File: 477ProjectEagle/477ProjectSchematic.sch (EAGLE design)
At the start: 67 parts, among them J1 POWER_JACK_BAT, J2 POWER_JACK_12VOUT, Q1 AO4419, X1 22-23-2051, X10 MOTORS, X2 XRJK-S-01-6-6-0-2G2-NO

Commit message: Scott lab -- Work on main PCB
Started connecting everything together. Made a bunch of progress.
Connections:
- net +3V3: now also X1-1.S; no longer X1-2.S
- net GND: now also X1-2.S; no longer X1-1.S
- net N$12: now also U$3.A1
- net N$13: now also U$3.A2
- net N$8: now also U$19.A8; no longer U$19.A7
- net N$9: now also U$19.A7; no longer U$19.A8
- net SCL: now also U$3.B1
- net SDA: now also U$3.B2
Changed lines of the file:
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@@
 <instance part="SUPPLY38" gate="+5V" x="-83.82" y="7.62"/>
 <instance part="SUPPLY39" gate="GND" x="-86.36" y="-5.08"/>
-<instance part="SUPPLY40" gate="GND" x="-426.72" y="10.16"/>
+<instance part="SUPPLY40" gate="GND" x="-429.26" y="10.16"/>
 <instance part="+3V2" gate="G$1" x="-132.08" y="73.66"/>
 <instance part="+3V3" gate="G$1" x="-167.64" y="-12.7"/>
@@
 <segment>
 <pinref part="U$1" gate="A" pin="U1RX/SDI1/RF2"/>
-<wire x1="76.2" y1="-27.94" x2="83.82" y2="-27.94" width="0.1524" layer="91"/>
-<wire x1="83.82" y1="-27.94" x2="99.06" y2="-27.94" width="0.1524" layer="91"/>
-<wire x1="99.06" y1="-27.94" x2="99.06" y2="33.02" width="0.1524" layer="91"/>
-<pinref part="U$19" gate="G$1" pin="A7"/>
-<wire x1="99.06" y1="33.02" x2="106.68" y2="33.02" width="0.1524" layer="91"/>
+<wire x1="76.2" y1="-27.94" x2="99.06" y2="-27.94" width="0.1524" layer="91"/>
+<wire x1="99.06" y1="-27.94" x2="99.06" y2="30.48" width="0.1524" layer="91"/>
 <junction x="76.2" y="-27.94"/>
-<junction x="106.68" y="33.02"/>
+<pinref part="U$19" gate="G$1" pin="A8"/>
+<wire x1="99.06" y1="30.48" x2="106.68" y2="30.48" width="0.1524" layer="91"/>
+<junction x="106.68" y="30.48"/>
 </segment>
 </net>
 <net name="N$9" class="0">
 <segment>
-<wire x1="81.28" y1="-30.48" x2="76.2" y2="-30.48" width="0.1524" layer="91"/>
-<pinref part="U$19" gate="G$1" pin="A8"/>
 <wire x1="76.2" y1="-30.48" x2="73.66" y2="-30.48" width="0.1524" layer="91"/>
-<wire x1="106.68" y1="30.48" x2="101.6" y2="30.48" width="0.1524" layer="91"/>
-<wire x1="101.6" y1="30.48" x2="101.6" y2="-30.48" width="0.1524" layer="91"/>
-<wire x1="101.6" y1="-30.48" x2="81.28" y2="-30.48" width="0.1524" layer="91"/>
+<wire x1="101.6" y1="33.02" x2="101.6" y2="-30.48" width="0.1524" layer="91"/>
+<wire x1="101.6" y1="-30.48" x2="76.2" y2="-30.48" width="0.1524" layer="91"/>
 <pinref part="U$1" gate="A" pin="U1TX/SDO1/RF3"/>
 <junction x="76.2" y="-30.48"/>
-<junction x="106.68" y="30.48"/>
+<pinref part="U$19" gate="G$1" pin="A7"/>
+<wire x1="101.6" y1="33.02" x2="106.68" y2="33.02" width="0.1524" layer="91"/>
+<junction x="106.68" y="33.02"/>
 </segment>
 </net>
@@
 <wire x1="76.2" y1="-20.32" x2="132.08" y2="-20.32" width="0.1524" layer="91"/>
 <wire x1="132.08" y1="-20.32" x2="132.08" y2="-58.42" width="0.1524" layer="91"/>
-<wire x1="132.08" y1="-58.42" x2="144.78" y2="-58.42" width="0.1524" layer="91"/>
+<wire x1="132.08" y1="-58.42" x2="142.24" y2="-58.42" width="0.1524" layer="91"/>
 <junction x="76.2" y="-20.32"/>
+<pinref part="U$3" gate="G$1" pin="A1"/>
+<junction x="142.24" y="-58.42"/>
+<wire x1="142.24" y1="-58.42" x2="144.78" y2="-58.42" width="0.1524" layer="91"/>
 </segment>
 </net>
@@
 <wire x1="76.2" y1="-22.86" x2="129.54" y2="-22.86" width="0.1524" layer="91"/>
 <wire x1="129.54" y1="-22.86" x2="129.54" y2="-60.96" width="0.1524" layer="91"/>
-<wire x1="129.54" y1="-60.96" x2="144.78" y2="-60.96" width="0.1524" layer="91"/>
+<wire x1="129.54" y1="-60.96" x2="142.24" y2="-60.96" width="0.1524" layer="91"/>
 <pinref part="U$1" gate="A" pin="SDA1/RG3"/>
 <junction x="76.2" y="-22.86"/>
+<pinref part="U$3" gate="G$1" pin="A2"/>
+<junction x="142.24" y="-60.96"/>
+<wire x1="142.24" y1="-60.96" x2="144.78" y2="-60.96" width="0.1524" layer="91"/>
 </segment>
 </net>
@@
 <net name="SCL" class="0">
 <segment>
-<wire x1="170.18" y1="-58.42" x2="203.2" y2="-58.42" width="0.1524" layer="91"/>
-<pinref part="ENCODER" gate="-1" pin="S"/>
-</segment>
-<segment>
 <pinref part="X1" gate="-4" pin="S"/>
 <wire x1="-431.8" y1="27.94" x2="-429.26" y2="27.94" width="0.2032" layer="91"/>
 <wire x1="-429.26" y1="27.94" x2="-416.56" y2="27.94" width="0.1524" layer="91"/>
+<junction x="-431.8" y="27.94"/>
+</segment>
+<segment>
+<pinref part="ENCODER" gate="-1" pin="S"/>
+<pinref part="U$3" gate="G$1" pin="B1"/>
+<wire x1="203.2" y1="-58.42" x2="172.72" y2="-58.42" width="0.1524" layer="91"/>
+<junction x="172.72" y="-58.42"/>
+<junction x="203.2" y="-58.42"/>
 </segment>
 </net>
 <net name="SDA" class="0">
-<segment>
-<wire x1="170.18" y1="-60.96" x2="203.2" y2="-60.96" width="0.1524" layer="91"/>
-<pinref part="ENCODER" gate="-2" pin="S"/>
-</segment>
 <segment>
 <pinref part="X1" gate="-3" pin="S"/>
 <wire x1="-431.8" y1="25.4" x2="-429.26" y2="25.4" width="0.2032" layer="91"/>
 <wire x1="-429.26" y1="25.4" x2="-416.56" y2="25.4" width="0.1524" layer="91"/>
+<junction x="-431.8" y="25.4"/>
+</segment>
+<segment>
+<pinref part="U$3" gate="G$1" pin="B2"/>
+<pinref part="ENCODER" gate="-2" pin="S"/>
+<wire x1="172.72" y1="-60.96" x2="203.2" y2="-60.96" width="0.1524" layer="91"/>
+<junction x="172.72" y="-60.96"/>
+<junction x="203.2" y="-60.96"/>
 </segment>
 </net>
@@
 <pinref part="U$42" gate="G$1" pin="2"/>
 <wire x1="124.46" y1="-71.12" x2="134.62" y2="-71.12" width="0.1524" layer="91"/>
+<junction x="142.24" y="-71.12"/>
 </segment>
 <segment>
@@
 </segment>
 <segment>
-<pinref part="X1" gate="-1" pin="S"/>
-<wire x1="-431.8" y1="20.32" x2="-426.72" y2="20.32" width="0.2032" layer="91"/>
-<wire x1="-426.72" y1="20.32" x2="-426.72" y2="12.7" width="0.2032" layer="91"/>
+<wire x1="-429.26" y1="20.32" x2="-429.26" y2="12.7" width="0.2032" layer="91"/>
 <pinref part="SUPPLY40" gate="GND" pin="GND"/>
+<pinref part="X1" gate="-2" pin="S"/>
+<wire x1="-431.8" y1="22.86" x2="-429.26" y2="22.86" width="0.1524" layer="91"/>
+<wire x1="-429.26" y1="22.86" x2="-429.26" y2="20.32" width="0.1524" layer="91"/>
+<junction x="-431.8" y="22.86"/>
 </segment>
 <segment>
@@
 <junction x="-149.86" y="-25.4"/>
 <pinref part="U$23" gate="G$1" pin="2"/>
+<junction x="-78.74" y="-12.7"/>
 </segment>
 <segment>
@@
 <pinref part="U$24" gate="G$1" pin="2"/>
 <junction x="-121.92" y="60.96"/>
+<junction x="-78.74" y="27.94"/>
 </segment>
 <segment>
@@
 <wire x1="-160.02" y1="-15.24" x2="-167.64" y2="-15.24" width="0.2032" layer="91"/>
 <wire x1="-160.02" y1="-15.24" x2="-160.02" y2="-17.78" width="0.1524" layer="91"/>
+<junction x="-160.02" y="-15.24"/>
 </segment>
 <segment>
@@
 </segment>
 <segment>
-<pinref part="X1" gate="-2" pin="S"/>
-<wire x1="-431.8" y1="22.86" x2="-426.72" y2="22.86" width="0.2032" layer="91"/>
 <wire x1="-426.72" y1="22.86" x2="-426.72" y2="30.48" width="0.2032" layer="91"/>
 <pinref part="+3V6" gate="G$1" pin="+3V3"/>
+<pinref part="X1" gate="-1" pin="S"/>
+<wire x1="-431.8" y1="20.32" x2="-426.72" y2="20.32" width="0.1524" layer="91"/>
+<wire x1="-426.72" y1="20.32" x2="-426.72" y2="22.86" width="0.1524" layer="91"/>
+<junction x="-431.8" y="20.32"/>
 </segment>
 <segment>
@@
 <wire x1="238.76" y1="127" x2="259.08" y2="127" width="0.1524" layer="91"/>
 <junction x="259.08" y="127"/>
+<junction x="218.44" y="96.52"/>
 </segment>
 </net>
@@
 <pinref part="SV4" gate="G$1" pin="1"/>
 <wire x1="104.14" y1="-40.64" x2="104.14" y2="-43.18" width="0.1524" layer="91"/>
-</segment>
-</net>
+<junction x="104.14" y="-43.18"/>
+</segment>
+</net>

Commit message: minor changes to main PCB
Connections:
- net N$85: now also U$1.PMBE/OC4/RD3
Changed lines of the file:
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@@
 <wire x1="91.44" y1="96.52" x2="33.02" y2="96.52" width="0.2032" layer="91"/>
 <wire x1="33.02" y1="96.52" x2="33.02" y2="15.24" width="0.2032" layer="91"/>
-<wire x1="33.02" y1="15.24" x2="73.66" y2="15.24" width="0.2032" layer="91"/>
-<junction x="73.66" y="15.24"/>
 <junction x="91.44" y="83.82"/>
+<pinref part="U$1" gate="A" pin="PMBE/OC4/RD3"/>
+<wire x1="33.02" y1="15.24" x2="76.2" y2="15.24" width="0.1524" layer="91"/>
+<junction x="76.2" y="15.24"/>
 </segment>
 </net>

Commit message: Did a lot of work on the PCB design
Added headers to pad out all micro pins. Routed pretty much everything
to where it needs to go. Just need to fix hbridge and check accuracy of
connections
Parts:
- removed SV1: (no value), con-lsta:FE08-1
- removed SV2: (no value), con-lsta:FE09-1
- removed SV3, SV4: (no value), con-lsta:FE10-1
- added SV5, SV6, SV7, SV8: (no value), con-lstb:MA08-2
- added U$5: 10k, MinotaurParts:R-US"
- added U$6: 10uF, MinotaurParts:C-US-1206
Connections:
- removed net N$31: U$1.PMA8/U2TX/SCL2/CN18/RF5
- removed net N$58: U$1.*MCLR, U$21.2, U$22.1, X2.1
- removed net N$62: U$1.TCK/PMA11/AN12/RB12
- removed net N$78: SV3.3
- removed net N$79: SV3.4
- removed net N$80: SV3.5
- removed net N$84: SV3.9, U$1.PMWR/OC5/IC5/CN13/RD4
- removed net N$85: SV3.10, U$1.PMBE/OC4/RD3
- new net N$90: SV6.15, U$1.PMA9/U2RX/SDA2/CN17/RF4
- new net N$91: SV5.8, U$1.PMA2/*SS2/CN11/RG9
- new net N$92: U$3.OE, U$5.1
- new net N$93: SV6.16, U$1.PMA8/U2TX/SCL2/CN18/RF5
- new net N$94: SV7.10, U$1.CN16/RD7
- new net N$95: SV7.7, U$1.RF0
- new net N$96: SV7.6, U$1.RF1
- new net N$97: SV7.5, U$1.PMD0/RE0
- new net N$98: SV7.8, U$1.ENVREG
- net +3V3: now also SV5.10, SV6.10, SV8.11, U$5.2
- net +5V: now also SV6.3, U$6.1
- net GND: now also SV5.9, SV6.4, SV6.9, SV8.8, U$6.2
- net N$1: now also SV5.11
- net N$10: now also SV6.1, U$1.PGC2/EMUC2/AN6/OCFA/RB6; no longer SV1.7, U$1.PMD6/RE6
- net N$11: now also SV5.2, U$1.PMD6/RE6; no longer SV1.6, U$1.PMD7/RE7
- net N$12: now also SV8.12
- net N$13: now also SV8.13
- net N$14: now also SV5.15
- net N$15: now also SV7.1
- net N$17: now also SV7.2
- net N$2: now also SV5.12
- net N$22: now also SV6.2, U$1.PGD2/EMUD2/AN7/RB7; no longer U$1.PMA0/AN15/OCFB/CN12/RB15, U$3.OE
- net N$23: now also SV5.3, U$1.PMD7/RE7; no longer SV1.5, U$1.PMA5/SCK2/CN8/RG6
- net N$24: now also SV5.4, U$1.PMA5/SCK2/CN8/RG6; no longer SV1.4, U$1.PMA4/SDI2/CN9/RG7
- net N$26: now also SV5.5, U$1.PMA4/SDI2/CN9/RG7; no longer SV1.3, U$1.PMA3/SDO2/CN10/RG8
- net N$27: now also SV5.6, U$1.PMA3/SDO2/CN10/RG8; no longer SV1.2, U$1.PMA2/*SS2/CN11/RG9
- net N$29: now also SV7.3
- net N$3: now also SV5.13
- net N$30: now also SV5.7, U$1.*MCLR, U$21.2, U$22.1, X2.1; no longer SV1.1, U$1.PGC2/EMUC2/AN6/OCFA/RB6
- net N$32: now also SV7.4
- net N$34: now also SV7.15
- net N$38: now also SV7.16
- net N$4: now also SV5.14
- net N$46: now also SV6.5, U$1.*U2CTS/C1OUT/AN8/RB8; no longer U$1.PMA9/U2RX/SDA2/CN17/RF4
- net N$5: now also SV6.6
- net N$57: now also SV6.7, U$1.TMS/PMA13/CVREF/AN10/RB10; no longer U$1.PMA1/*U2RTS/BCLK2/AN14/RB14
- net N$59: now also SV8.1, U$1.SOSCO/T1CK/CN0/RC14; no longer SV4.8, U$1.OSC2/CLKO/RC15
- net N$6: now also SV5.1; no longer SV1.8
- net N$61: now also SV6.8, U$1.TDO/PMA12/AN11/RB11; no longer SV2.4, U$1.TDI/PMA10/AN13/RB13
- net N$63: now also SV6.11, U$1.TCK/PMA11/AN12/RB12; no longer U$1.TDO/PMA12/AN11/RB11
- net N$64: now also SV6.12, U$1.TDI/PMA10/AN13/RB13; no longer SV2.7, U$1.TMS/PMA13/CVREF/AN10/RB10
- net N$65: now also SV6.13, U$1.PMA1/*U2RTS/BCLK2/AN14/RB14; no longer U$1.*U2CTS/C1OUT/AN8/RB8
- net N$66: now also SV6.14, U$1.PMA0/AN15/OCFB/CN12/RB15; no longer U$1.PGD2/EMUD2/AN7/RB7
- net N$67: now also SV7.9, U$1.VCAP/VDDCORE; no longer SV4.10, U$1.*U1RTS/BCLK1/SCK1/INT0/RF6
- net N$68: now also SV8.2, U$1.SOSCI/CN1/RC13; no longer SV4.9, U$1.OSC1/CLKI/RC12
- net N$69: now also SV8.3, U$1.OC1/RD0; no longer SV4.7, U$1.IC1/RTCC/INT1/RD8
- net N$7: now also SV5.16
- net N$70: now also SV8.4, U$1.IC4/PMCS1/INT4/RD11; no longer SV4.6, U$1.IC2/*U1CTS/INT2/RD9
- net N$71: now also SV8.5; no longer SV4.5
- net N$72: now also SV8.6, U$1.IC2/*U1CTS/INT2/RD9; no longer SV4.4, U$1.IC4/PMCS1/INT4/RD11
- net N$73: now also SV8.7, U$1.IC1/RTCC/INT1/RD8; no longer SV4.3, U$1.OC1/RD0
- net N$74: now also SV8.9, U$1.OSC2/CLKO/RC15; no longer SV4.2, U$1.SOSCI/CN1/RC13
- net N$75: now also SV8.10, U$1.OSC1/CLKI/RC12; no longer SV4.1, U$1.SOSCO/T1CK/CN0/RC14
- net N$76: now also SV7.11, U$1.CN15/RD6; no longer SV3.1, U$1.PMD0/RE0
- net N$77: now also SV7.12, U$1.PMRD/CN14/RD5; no longer SV3.2
- net N$8: now also SV8.15
- net N$81: now also SV7.13, U$1.PMWR/OC5/IC5/CN13/RD4; no longer SV3.6
- net N$82: now also SV7.14, U$1.PMBE/OC4/RD3; no longer SV3.7, U$1.CN15/RD6
- net N$83: now also SV8.14, U$1.*U1RTS/BCLK1/SCK1/INT0/RF6; no longer SV3.8, U$1.PMRD/CN14/RD5
- net N$9: now also SV8.16
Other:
- moved on the sheet: ENCODER-1, ENCODER-2, SW_1, U$19, U$2, U$20, U$21, U$23, U$25, U$3, U$39, U$40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

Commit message: Scott Lab - PCB All connected
Added kickback diodes to the HBridge circuit. Added power LED and status
LED. Changed all external connectors to parts from the sparkfun library
(DB9, barrel, RJ11). Need to add more silkscreen - label all
connectionsto outside
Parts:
- removed X2: XRJK-S-01-6-6-0-2G2-NO, con-xmultiple:XRJK-S-01-6-6-0-2G2-NO
- removed X3: (no value), con-subd:F09HP
- added D1, D2, D3, D4, D5, D6, D7, D8: (no value), diode:DIODE-DO-214AC
- added J3: RJ11-6PTH, SparkFun-Connectors:RJ11-6PTH
- added LED1, POWER: (no value), led:LEDSMT1206
- added RLED, RLED2: 1k, MinotaurParts:R-US"
- added X4: (no value), SparkFun-Connectors:DB9FEMALE
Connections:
- new net N$31: LED1.A, RLED.2
- new net N$78: POWER.A, RLED2.2
- net +3V3: now also J3.2, RLED2.1; no longer X2.2
- net +7V: now also D4.C, D5.C, D7.C, D8.C
- net GND: now also D1.A, D2.A, D3.A, D6.A, LED1.C, POWER.C, U$2.SA, U$2.SB, X4.1; no longer X3.1
- net N$14: now also J3.5; no longer X2.5
- net N$18: now also D2.C, D8.A
- net N$19: now also D1.C, D7.A
- net N$20: now also D5.A, D6.C
- net N$21: now also D3.C, D4.A
- net N$30: now also J3.1; no longer X2.1
- net N$53: now also X4.2; no longer X3.2
- net N$66: now also RLED.1
- net N$7: now also J3.4; no longer X2.4
- net N$86: now also J3.3; no longer X2.3
- net N$87: now also X4.3; no longer X3.3

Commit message: Changes to main PCB!!!
Took out I2C level converter. Changed encoder to GPIO pins
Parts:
- removed U$3: TXS0104E, MinotaurParts:TXS0104E
- removed U$41, U$42: 10uF, MinotaurParts:C-US-1206
- removed U$5: 10k, MinotaurParts:R-US"
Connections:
- removed net N$12: SV8.12, U$1.SCL1/RG2, U$3.A1
- removed net N$13: SV8.13, U$1.SDA1/RG3, U$3.A2
- removed net N$92: U$3.OE, U$5.1
- net +3V3: no longer U$3.VCCA, U$41.1, U$5.2
- net +5V: no longer U$3.VCCB, U$42.1
- net GND: no longer U$3.GND, U$41.2, U$42.2
- net N$70: now also ENCODER-1.S
- net N$71: now also ENCODER-2.S
- net SCL: now also SV8.12, U$1.SCL1/RG2; no longer ENCODER-1.S, U$3.B1
- net SDA: now also SV8.13, U$1.SDA1/RG3; no longer ENCODER-2.S, U$3.B2
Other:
- moved on the sheet: X1-1, X1-2, X1-3, X1-4

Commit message: Fixed Schematic to include cap for internal reg
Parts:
- added U$3: 10uF, MinotaurParts:C-US-1206
- U$23, U$24, U$25, U$40, U$43, U$44, U$6: value 10uF -> 0.1uF
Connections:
- removed net N$98: SV7.8, U$1.ENVREG
- net +3V3: now also SV7.8, U$1.ENVREG
- net GND: now also U$3.2
- net N$67: now also U$3.1
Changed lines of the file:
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@@
 <part name="CIN7" library="MinotaurParts" deviceset="C-US-1210" device="" value="10uF"/>
 <part name="L1_7" library="MinotaurParts" deviceset="SRR1210" device="" value="12uH"/>
-<part name="U$23" library="MinotaurParts" deviceset="C-US-1206" device="" value="10uF"/>
-<part name="U$24" library="MinotaurParts" deviceset="C-US-1206" device="" value="10uF"/>
-<part name="U$25" library="MinotaurParts" deviceset="C-US-1206" device="" value="10uF"/>
+<part name="U$23" library="MinotaurParts" deviceset="C-US-1206" device="" value="0.1uF"/>
+<part name="U$24" library="MinotaurParts" deviceset="C-US-1206" device="" value="0.1uF"/>
+<part name="U$25" library="MinotaurParts" deviceset="C-US-1206" device="" value="0.1uF"/>
 <part name="SUPPLY45" library="supply2" deviceset="GND" device=""/>
-<part name="U$40" library="MinotaurParts" deviceset="C-US-1206" device="" value="10uF"/>
-<part name="U$43" library="MinotaurParts" deviceset="C-US-1206" device="" value="10uF"/>
-<part name="U$44" library="MinotaurParts" deviceset="C-US-1206" device="" value="10uF"/>
+<part name="U$40" library="MinotaurParts" deviceset="C-US-1206" device="" value="0.1uF"/>
+<part name="U$43" library="MinotaurParts" deviceset="C-US-1206" device="" value="0.1uF"/>
+<part name="U$44" library="MinotaurParts" deviceset="C-US-1206" device="" value="0.1uF"/>
 <part name="SUPPLY46" library="supply2" deviceset="GND" device=""/>
 <part name="SUPPLY47" library="supply2" deviceset="GND" device=""/>
@@
 <part name="SV7" library="con-lstb" deviceset="MA08-2" device=""/>
 <part name="SV8" library="con-lstb" deviceset="MA08-2" device=""/>
-<part name="U$6" library="MinotaurParts" deviceset="C-US-1206" device="" value="10uF"/>
+<part name="U$6" library="MinotaurParts" deviceset="C-US-1206" device="" value="0.1uF"/>
 <part name="SUPPLY51" library="supply2" deviceset="GND" device=""/>
 <part name="D1" library="diode" deviceset="DIODE-" device="DO-214AC"/>
@@
 <part name="+3V10" library="supply1" deviceset="+3V3" device=""/>
 <part name="SUPPLY61" library="supply2" deviceset="GND" device=""/>
+<part name="U$3" library="MinotaurParts" deviceset="C-US-1206" device="" value="10uF"/>
+<part name="SUPPLY26" library="supply2" deviceset="GND" device=""/>
+<part name="+3V1" library="supply1" deviceset="+3V3" device=""/>
 </parts>
 <sheets>
@@
 <instance part="+3V10" gate="G$1" x="-386.08" y="43.18"/>
 <instance part="SUPPLY61" gate="GND" x="-386.08" y="15.24"/>
+<instance part="U$3" gate="G$1" x="118.11" y="59.69"/>
+<instance part="SUPPLY26" gate="GND" x="121.92" y="52.07"/>
+<instance part="+3V1" gate="G$1" x="83.82" y="64.77"/>
 </instances>
 <busses>
@@
 <junction x="-386.08" y="17.78"/>
 </segment>
+<segment>
+<pinref part="SUPPLY26" gate="GND" pin="GND"/>
+<junction x="121.92" y="54.61"/>
+<pinref part="U$3" gate="G$1" pin="2"/>
+<wire x1="118.11" y1="54.61" x2="121.92" y2="54.61" width="0.1524" layer="91"/>
+</segment>
 </net>
 <net name="N$16" class="0">
@@
 <pinref part="+3V10" gate="G$1" pin="+3V3"/>
 <junction x="-386.08" y="40.64"/>
+</segment>
+<segment>
+<wire x1="93.98" y1="30.48" x2="93.98" y2="33.02" width="0.1524" layer="91"/>
+<pinref part="SV7" gate="G$1" pin="8"/>
+<wire x1="93.98" y1="33.02" x2="123.19" y2="33.02" width="0.1524" layer="91"/>
+<wire x1="123.19" y1="33.02" x2="123.19" y2="34.29" width="0.1524" layer="91"/>
+<junction x="123.19" y="34.29"/>
+<pinref part="U$1" gate="A" pin="ENVREG"/>
+<wire x1="93.98" y1="30.48" x2="83.82" y2="30.48" width="0.1524" layer="91"/>
+<junction x="76.2" y="30.48"/>
+<wire x1="83.82" y1="30.48" x2="76.2" y2="30.48" width="0.1524" layer="91"/>
+<wire x1="83.82" y1="30.48" x2="83.82" y2="62.23" width="0.1524" layer="91"/>
+<pinref part="+3V1" gate="G$1" pin="+3V3"/>
+<junction x="83.82" y="62.23"/>
+<junction x="83.82" y="30.48"/>
 </segment>
 </net>
@@
 <wire x1="95.25" y1="27.94" x2="95.25" y2="31.75" width="0.1524" layer="91"/>
 <pinref part="SV7" gate="G$1" pin="9"/>
-<wire x1="95.25" y1="31.75" x2="107.95" y2="31.75" width="0.1524" layer="91"/>
+<wire x1="95.25" y1="31.75" x2="104.14" y2="31.75" width="0.1524" layer="91"/>
 <junction x="107.95" y="31.75"/>
 <pinref part="U$1" gate="A" pin="VCAP/VDDCORE"/>
+<wire x1="104.14" y1="31.75" x2="107.95" y2="31.75" width="0.1524" layer="91"/>
 <wire x1="95.25" y1="27.94" x2="76.2" y2="27.94" width="0.1524" layer="91"/>
 <junction x="76.2" y="27.94"/>
+<wire x1="104.14" y1="31.75" x2="104.14" y2="64.77" width="0.1524" layer="91"/>
+<wire x1="104.14" y1="64.77" x2="118.11" y2="64.77" width="0.1524" layer="91"/>
+<wire x1="118.11" y1="64.77" x2="118.11" y2="62.23" width="0.1524" layer="91"/>
+<junction x="104.14" y="31.75"/>
+<pinref part="U$3" gate="G$1" pin="1"/>
+<junction x="118.11" y="62.23"/>
 </segment>
 </net>
@@
 </segment>
 </net>
-<net name="N$98" class="0">
-<segment>
-<wire x1="93.98" y1="30.48" x2="93.98" y2="33.02" width="0.1524" layer="91"/>
-<pinref part="SV7" gate="G$1" pin="8"/>
-<wire x1="93.98" y1="33.02" x2="123.19" y2="33.02" width="0.1524" layer="91"/>
-<wire x1="123.19" y1="33.02" x2="123.19" y2="34.29" width="0.1524" layer="91"/>
-<junction x="123.19" y="34.29"/>
-<pinref part="U$1" gate="A" pin="ENVREG"/>
-<wire x1="93.98" y1="30.48" x2="76.2" y2="30.48" width="0.1524" layer="91"/>
-<junction x="76.2" y="30.48"/>
-</segment>
-</net>

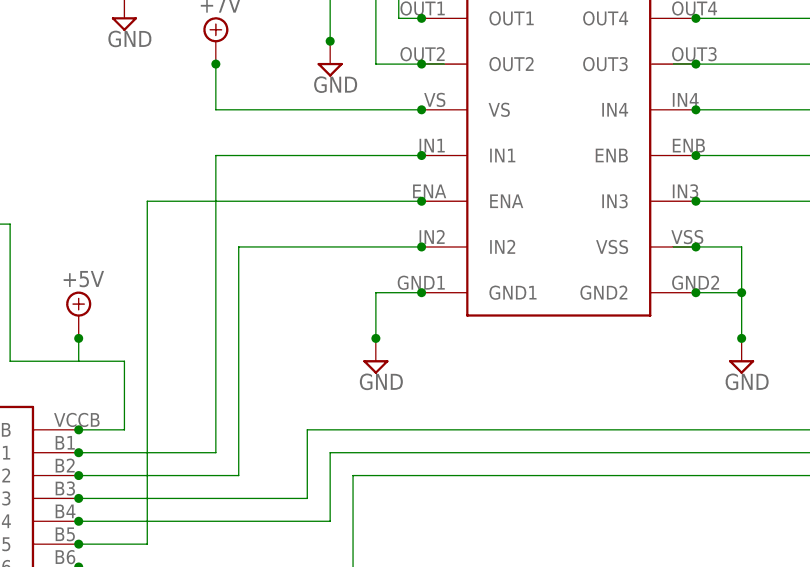
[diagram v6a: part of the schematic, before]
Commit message: Worked on PIC software
Implemented a circular send and receive buffer for the UART. Tested it
and got it working. Fixed the H-Bridge package. Wrote a txt document
with all the things that need to be fixed on the PCB.
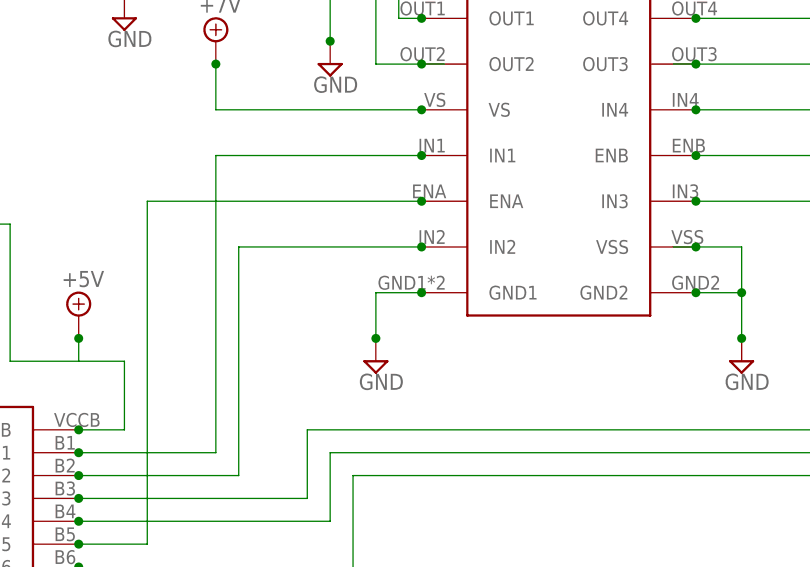
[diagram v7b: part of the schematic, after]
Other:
- moved on the sheet: U$2
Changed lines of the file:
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@@
 <setting verticaltext="up"/>
 </settings>
-<grid distance="0.05" unitdist="inch" unit="inch" style="lines" multiple="1" display="no" altdistance="0.01" altunitdist="inch" altunit="inch"/>
+<grid distance="0.1" unitdist="inch" unit="inch" style="lines" multiple="1" display="no" altdistance="0.01" altunitdist="inch" altunit="inch"/>
 <layers>
 <layer number="1" name="Top" color="4" fill="1" visible="no" active="no"/>
